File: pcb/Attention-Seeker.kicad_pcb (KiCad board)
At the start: 2 copper layers, 91 x 80.5 mm, 21 parts, among them Q1 BSS84, SW1 RotaryEncoder_Switch, SW2 SW_Push, SW3 SW_Push, SW4 SW_Push, U1 TFT_320x240, U2 ESP32-S3-DevKitC, U3 IRLML2502TRPBF, U4 AMS1117-3.3

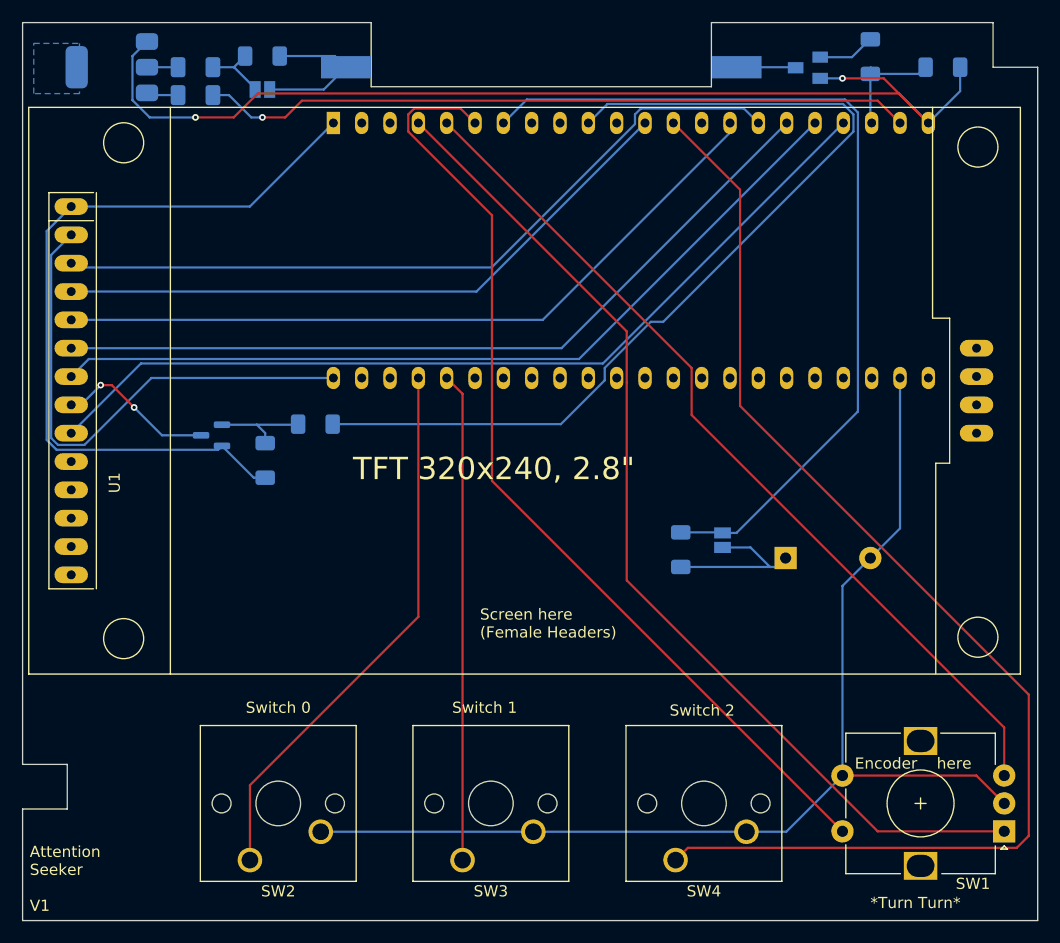
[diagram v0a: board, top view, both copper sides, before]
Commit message: changed pads for MCU and screen to fit square pins, 1mm hole diameter. Found cheaper MCU alternative. Moved MCU more to the edge and rerouted accordingly.
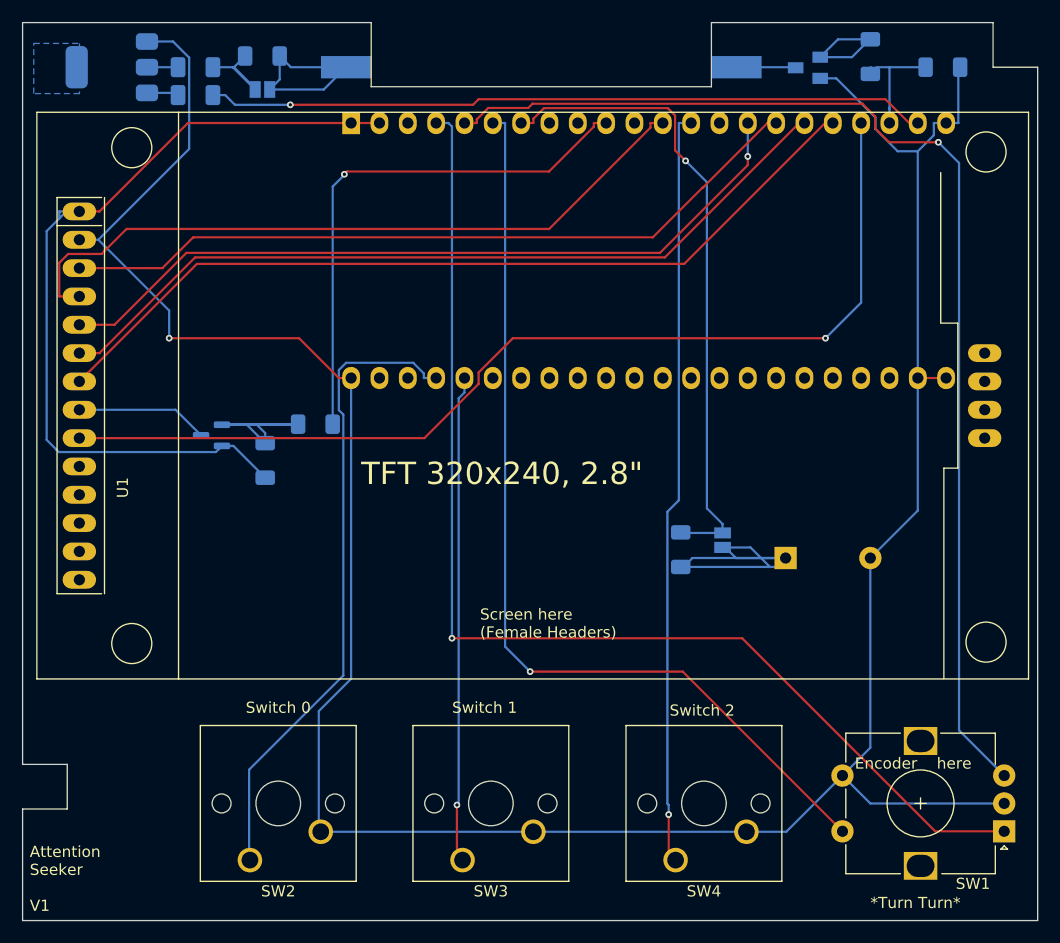
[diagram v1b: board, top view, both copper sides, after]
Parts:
- moved U2 1.59 mm to (77.0, 93.5)
- moved U1 0.85 mm to (52.6, 117.9)
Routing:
- net Net-(U2-GPIO3/ADC1_CH2): track 109.7 -> 67.9 mm, vias 0 -> 1
- net Net-(U2-GPIO17/ADC2_CH6): track 84.6 -> 48.4 mm, vias 0 -> 1
- net /DT: track 79.2 -> 104.7 mm, vias 0 -> 1
- net Net-(JP2-A): track 80.4 -> 57.8 mm, vias 0 -> 1
- net Net-(BZ1-+): track 14.7 -> 30.5 mm
- net /CLk: track 91.9 -> 104.1 mm, vias 0 -> 1
- net Net-(Q1-G): track 8.81 -> 20.2 mm
- net Net-(U1-MISO): track 80.7 -> 91.8 mm, vias 0 -> 1
- net Net-(U2-GPIO1/ADC1_CH0): track 49.5 -> 57.4 mm
- net Net-(U1-RST): track 57.7 -> 64.4 mm
- net +3.3V: track 70.3 -> 76.5 mm
- net Net-(U3-G): track 5.18 -> 10.3 mm
- net Net-(D1-A): track 14.0 -> 17.4 mm
- net Net-(U1-DC): track 66.9 -> 69.8 mm, vias 0 -> 1
- net Net-(JP1-A): track 6.09 -> 8.92 mm
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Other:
- board text added: "ESP32 S3 N16R8 CP2102 HERE"
- board text removed: "ESP HERE"

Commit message: Fixed some routing weirdness (unessecary paths) and added nearly fitting model for the mcu. Updated pictures and 3d Model
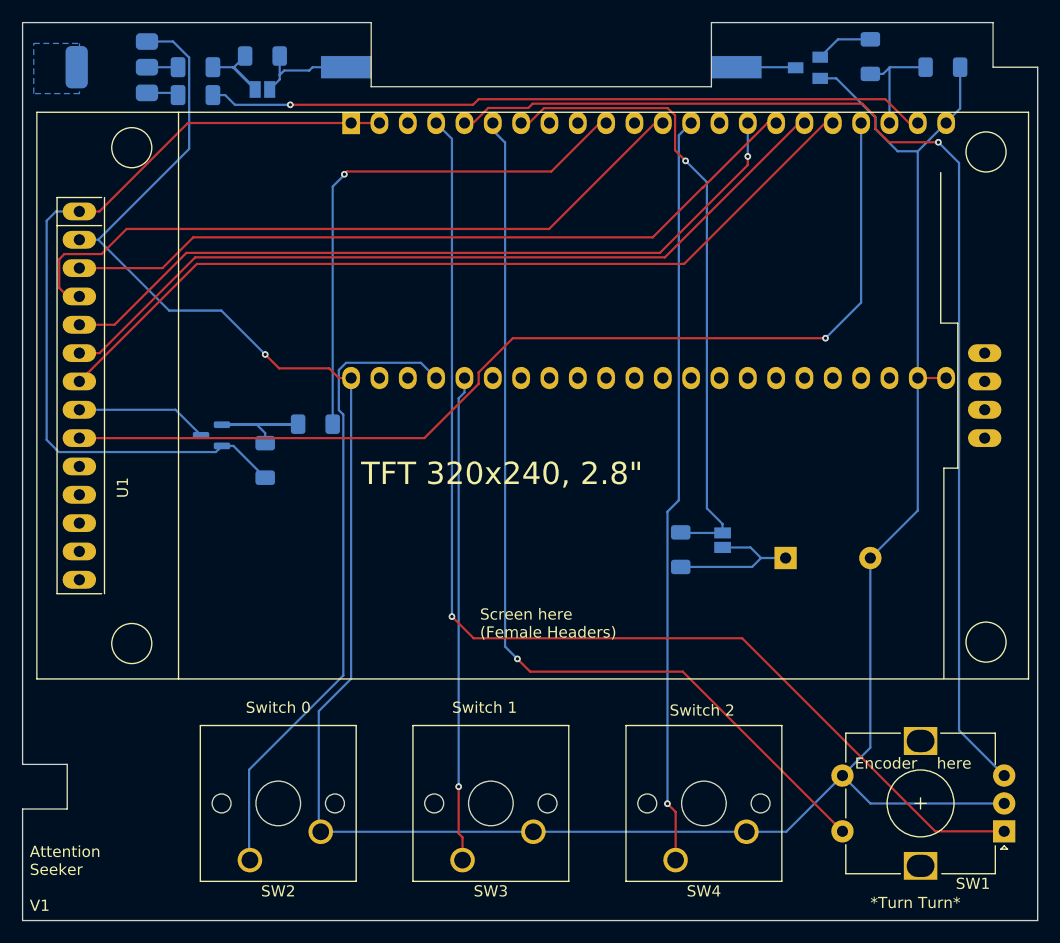
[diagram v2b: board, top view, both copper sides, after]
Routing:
- net Net-(BZ1-+): track 30.5 -> 15.0 mm
- net Net-(D1-A): track 17.4 -> 9.61 mm
- net Net-(U3-G): track 10.3 -> 5.16 mm
- net Net-(Q1-G): track 20.2 -> 17.9 mm
- net GND: track 245.2 -> 243.2 mm
- net /CLk: track 104.1 -> 102.3 mm
- net +3.3V: track 76.5 -> 75.1 mm
- net /SW: track 85.1 -> 84.5 mm
- net Net-(U2-GPIO2/ADC1_CH1): track 43.7 -> 44.3 mm

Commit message: updated rotary encoder footprint and sourced smd parts from other source
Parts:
- SW1: footprint Rotary_Encoder:RotaryEncoder_Alps_EC12E-Switch_Vertical_H20mm -> Rotary_Encoder:RotaryEncoder_Alps_EC11E-Switch_Vertical_H20mm
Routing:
- net /SW: track 84.5 -> 82.4 mm
- net GND: track 243.2 -> 242.7 mm
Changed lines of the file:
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@@
 		(tags "Cherry MX keyswitch 1.00u PCB")
 		(property "Reference" "SW3"
-			(at -2.54 -2.794 0)
+			(at -8.26 -2.82 0)
 			(layer "F.SilkS")
 			(effects
@@
 		(tags "Cherry MX keyswitch 1.00u PCB")
 		(property "Reference" "SW4"
-			(at -2.54 -2.794 0)
+			(at -8.16 -3.02 0)
 			(layer "F.SilkS")
 			(effects
@@
 		(tags "Cherry MX keyswitch 1.00u PCB")
 		(property "Reference" "SW2"
-			(at -2.54 -2.794 0)
+			(at -8.12 -3.02 0)
 			(layer "F.SilkS")
 			(effects
@@
 		)
 	)
-	(footprint "Rotary_Encoder:RotaryEncoder_Alps_EC12E-Switch_Vertical_H20mm"
+	(footprint "Rotary_Encoder:RotaryEncoder_Alps_EC11E-Switch_Vertical_H20mm"
 		(layer "F.Cu")
 		(at 135.5 157 180)
-		(descr "Alps rotary encoder, EC12E... with switch, vertical shaft, http://www.alps.com/prod/info/E/HTML/Encoder/Incremental/EC12E/EC12E1240405.html & http://cdn-reichelt.de/documents/datenblatt/F100/402097STEC12E08.PDF")
+		(descr "Alps rotary encoder, EC11E... with switch, vertical shaft, http://www.alps.com/prod/info/E/HTML/Encoder/Incremental/EC11/EC11E15204A3.html")
 		(tags "rotary encoder")
 		(property "Reference" "SW1"
-			(at 2.8 -4.7 0)
+			(at 0.3 -5.6 180)
 			(layer "F.SilkS")
 			(effects
@@
 		)
 		(property "Value" "RotaryEncoder_Switch"
-			(at 7.5 10.4 0)
+			(at 7.5 10.4 180)
 			(layer "F.Fab")
 			(effects
@@
 		(attr through_hole)
 		(fp_line
-			(start 14.2 8.8)
-			(end 9.3 8.8)
+			(start 13.6 8.4)
+			(end 9.5 8.4)
 			(stroke
 				(width 0.12)
@@
 		)
 		(fp_line
-			(start 14.2 6.2)
-			(end 14.2 8.8)
+			(start 13.6 6)
+			(end 13.6 8.4)
 			(stroke
 				(width 0.12)
@@
 		)
 		(fp_line
-			(start 14.2 1.2)
-			(end 14.2 3.8)
+			(start 13.6 1.2)
+			(end 13.6 3.8)
 			(stroke
 				(width 0.12)
@@
 		)
 		(fp_line
-			(start 14.2 -3.8)
-			(end 14.2 -1.2)
+			(start 13.6 -3.4)
+			(end 13.6 -1)
 			(stroke
 				(width 0.12)
@@
 		)
 		(fp_line
-			(start 9.3 -3.8)
-			(end 14.2 -3.8)
+			(start 9.5 -3.4)
+			(end 13.6 -3.4)
 			(stroke
 				(width 0.12)
@@
 		)
 		(fp_line
-			(start 5.7 8.8)
-			(end 0.8 8.8)
-			(stroke
-				(width 0.12)
-				(type solid)
-			)
-			(layer "F.SilkS")
-		)
-		(fp_line
-			(start 5.6 -3.8)
-			(end 0.8 -3.8)
+			(start 5.5 8.4)
+			(end 1.4 8.4)
 			(stroke
 				(width 0.12)
@@
 		)
 		(fp_line
-			(start 0.8 8.8)
-			(end 0.8 6)
+			(start 5.5 -3.4)
+			(end 1.4 -3.4)
 			(stroke
 				(width 0.12)
@@
 		)
 		(fp_line
-			(start 0.8 -3.8)
-			(end 0.8 -1.3)
+			(start 1.4 -3.4)
+			(end 1.4 8.4)
 			(stroke
 				(width 0.12)
@@
 		)
 		(fp_line
-			(start 16 9.85)
-			(end 16 -4.85)
+			(start 16 9.6)
+			(end 16 -4.6)
 			(stroke
 				(width 0.05)
@@
 		)
 		(fp_line
-			(start 16 9.85)
-			(end -1.5 9.85)
+			(start 16 9.6)
+			(end -1.5 9.6)
 			(stroke
 				(width 0.05)
@@
 		)
 		(fp_line
-			(start -1.5 -4.85)
-			(end 16 -4.85)
+			(start -1.5 -4.6)
+			(end 16 -4.6)
 			(stroke
 				(width 0.05)
@@
 		)
 		(fp_line
-			(start -1.5 -4.85)
-			(end -1.5 9.85)
+			(start -1.5 -4.6)
+			(end -1.5 9.6)
 			(stroke
 				(width 0.05)
@@
 		)
 		(fp_line
-			(start 14.1 8.7)
-			(end 0.9 8.7)
+			(start 13.5 8.3)
+			(end 1.5 8.3)
 			(stroke
 				(width 0.12)
@@
 		)
 		(fp_line
-			(start 14.1 -3.7)
-			(end 14.1 8.7)
+			(start 13.5 -3.3)
+			(end 13.5 8.3)
 			(stroke
 				(width 0.12)
@@
 		)
 		(fp_line
-			(start 1.9 -3.7)
-			(end 14.1 -3.7)
+			(start 2.5 -3.3)
+			(end 13.5 -3.3)
 			(stroke
 				(width 0.12)
@@
 		)
 		(fp_line
-			(start 0.9 8.7)
-			(end 0.9 -2.6)
+			(start 1.5 8.3)
+			(end 1.5 -2.2)
 			(stroke
 				(width 0.12)
@@
 		)
 		(fp_line
-			(start 0.9 -2.6)
-			(end 1.9 -3.7)
+			(start 1.5 -2.2)
+			(end 2.5 -3.3)
 			(stroke
 				(width 0.12)
@@
 		)
 		(fp_text user "${REFERENCE}"
-			(at 11.5 6.6 0)
+			(at 11.1 6.3 180)
 			(layer "F.Fab")
 			(effects
@@
 		(pad "MP" thru_hole rect
 			(at 7.5 -3.1 180)
-			(size 3 2.5)
-			(drill oval 2.5 2)
+			(size 3.2 2)
+			(drill oval 2.8 1.5)
 			(layers "*.Cu" "*.Mask")
 			(remove_unused_layers no)
@@
 		(pad "MP" thru_hole rect
 			(at 7.5 8.1 180)
-			(size 3 2.5)
-			(drill oval 2.5 2)
+			(size 3.2 2)
+			(drill oval 2.8 1.5)
 			(layers "*.Cu" "*.Mask")
 			(remove_unused_layers no)
 		)
 		(pad "S1" thru_hole circle
-			(at 14.5 0 180)
+			(at 14.5 5 180)
 			(size 2 2)
 			(drill 1)
@@
 		)
 		(pad "S2" thru_hole circle
-			(at 14.5 5 180)
+			(at 14.5 0 180)
 			(size 2 2)
 			(drill 1)
@@
 		)
 		(embedded_fonts no)
-		(model "${KIPRJMOD}/models/rotary-encoder/旋转编码器.STEP"
+		(model "${KICAD9_3DMODEL_DIR}/Rotary_Encoder.3dshapes/RotaryEncoder_Alps_EC11E-Switch_Vertical_H20mm.step"
 			(offset
-				(xyz 7.5 -2.5 0)
+				(xyz 0 0 0)
 			)
 			(scale
@@
 			)
 			(rotate
-				(xyz -90 -0 -90)
+				(xyz 0 0 0)
 			)
 		)
@@
 	)
 	(gr_text "Encoder"
-		(at 122.1 151.5 0)
+		(at 125 151.4 0)
 		(layer "F.SilkS")
 		(effects
@@
 	)
 	(gr_text "here"
-		(at 129.45 151.5 0)
+		(at 126.2 158.6 0)
 		(layer "F.SilkS")
 		(effects
@@
 	)
 	(segment
+		(start 123.5 132.5)
+		(end 123.5 154.4)
+		(width 0.2)
+		(layer "B.Cu")
+		(net 6)
+	)
+	(segment
 		(start 58.65 86.2)
 		(end 60.9871 86.2)
@@
 	)
 	(segment
+		(start 123.5 154.5)
+		(end 121 157)
+		(width 0.2)
+		(layer "B.Cu")
+		(net 6)
+	)
+	(segment
 		(start 74.0523 156.8623)
 		(end 74.23 157.04)
@@
 	)
 	(segment
+		(start 120.96 157.04)
+		(end 121 157)
+		(width 0.2)
+		(layer "B.Cu")
+		(net 6)
+	)
+	(segment
 		(start 130.28998 93.46002)
 		(end 131.55 92.2)
@@
 	)
 	(segment
-		(start 121 152)
-		(end 123.5 154.5)
+		(start 123.5 154.4)
+		(end 123.6 154.5)
 		(width 0.2)
 		(layer "B.Cu")
@@
 	(segment
 		(start 123.5 154.5)
+		(end 123.6 154.5)
+		(width 0.2)
+		(layer "B.Cu")
+		(net 6)
+	)
+	(segment
+		(start 123.6 154.5)
 		(end 135.5 154.5)
 		(width 0.2)
@@
 	)
 	(segment
-		(start 112.39 157.04)
-		(end 115.96 157.04)
-		(width 0.2)
-		(layer "B.Cu")
-		(net 6)
-	)
-	(segment
 		(start 60.639 110.3181)
 		(end 54.2909 103.97)
@@
 	)
 	(segment
-		(start 121 152)
-		(end 123.5 149.5)
-		(width 0.2)
-		(layer "B.Cu")
-		(net 6)
-	)
-	(segment
 		(start 62.4339 95.827)
 		(end 54.2909 103.97)
@@
 	)
 	(segment
-		(start 123.9432 93.0002)
-		(end 123.9432 94.0298)
+		(start 112.39 157.04)
+		(end 120.96 157.04)
 		(width 0.2)
 		(layer "B.Cu")
@@
 	)
 	(segment
-		(start 119 89.5)
-		(end 120.443 89.5)
+		(start 123.9432 93.0002)
+		(end 123.9432 94.0298)
 		(width 0.2)
 		(layer "B.Cu")
@@
 	)
 	(segment
-		(start 115.96 157.04)
-		(end 121 152)
+		(start 119 89.5)
+		(end 120.443 89.5)
 		(width 0.2)
 		(layer "B.Cu")
@@
 	)
 	(segment
-		(start 123.5 149.5)
-		(end 123.5 132.5)
-		(width 0.2)
-		(layer "B.Cu")
-		(net 6)
-	)
-	(segment
 		(start 128.45 88.5)
 		(end 125.25 88.5)
@@
 	)
 	(segment
+		(start 116 152)
+		(end 106.6832 142.6832)
+		(width 0.2)
+		(layer "F.Cu")
+		(net 9)
+	)
+	(segment
 		(start 91.8589 141.5411)
 		(end 93.001 142.6832)
@@
 	)
 	(segment
-		(start 106.6832 142.6832)
-		(end 121 157)
+		(start 121 152)
+		(end 116 152)
 		(width 0.2)
 		(layer "F.Cu")

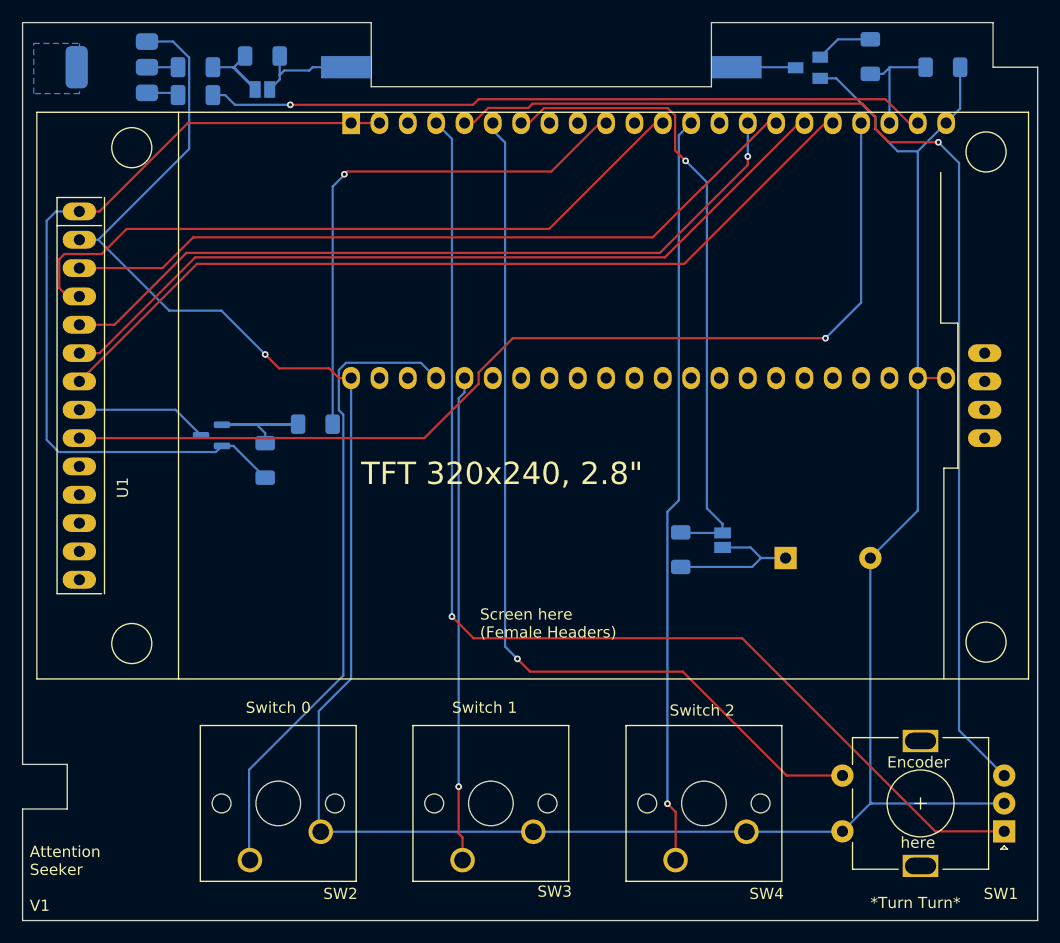
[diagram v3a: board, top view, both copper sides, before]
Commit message: fixed critical issue with cap alignment
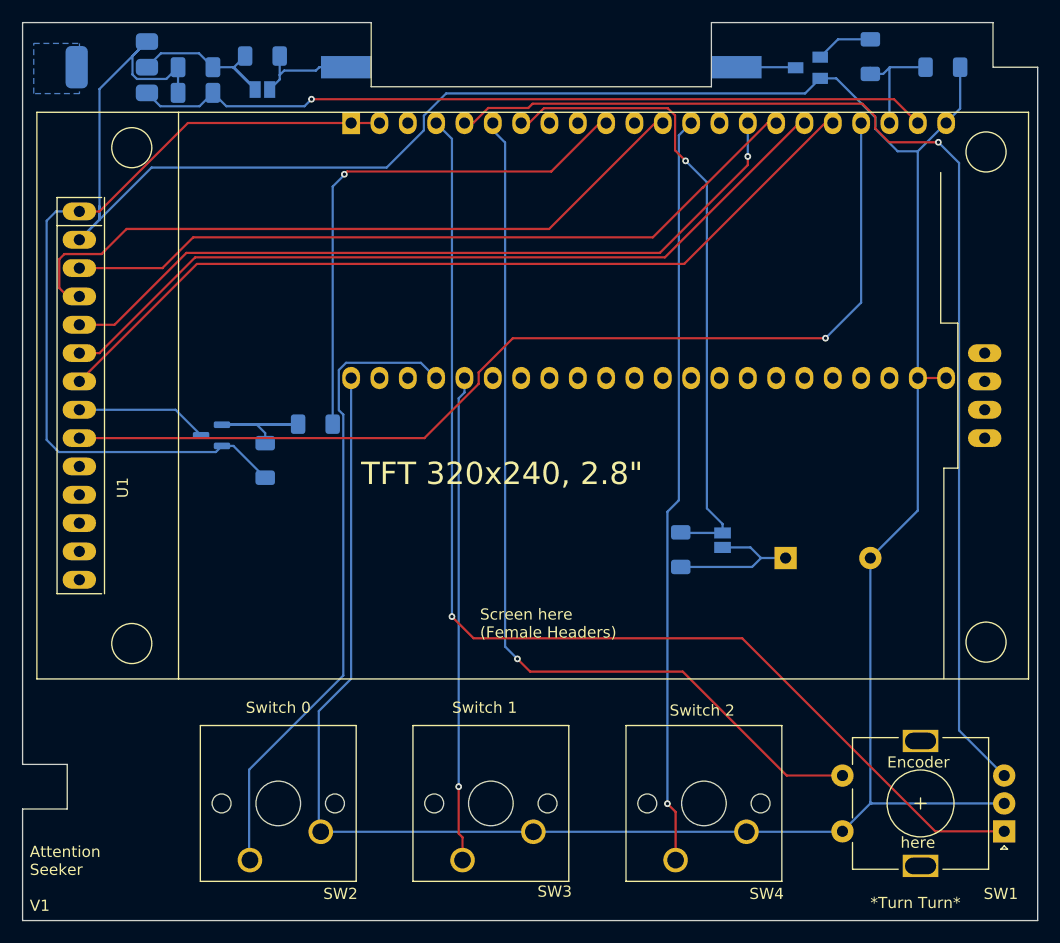
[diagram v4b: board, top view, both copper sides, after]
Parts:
- C2: value 100nC -> 10µC
- moved C1 0.20 mm to (63.0, 90.8), turned to 0 degrees
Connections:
- C1 pad 1: +5V -> GND
- C1 pad 2: Net-(U4-VI) -> +5V
- C2 pad 1: Net-(U4-VO) -> GND
- U4 pad 2: Net-(U4-VO) -> Net-(JP1-A)
- U4 pad 3: Net-(U4-VI) -> +5V
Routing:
- net GND: track 242.7 -> 294.2 mm, vias 1 -> 0
- net +5V: track 64.6 -> 71.7 mm
- net Net-(JP1-A): track 8.92 -> 15.9 mm
- net Net-(U4-VO): track 2.95 -> 0.00 mm
- net Net-(U4-VI): track 2.87 -> 0.00 mm
- added copper zone on B.Cu, net Net-(JP1-A)
- removed copper zone on B.Cu, net Net-(U4-VO)
